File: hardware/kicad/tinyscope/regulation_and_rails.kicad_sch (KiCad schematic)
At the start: 28 parts

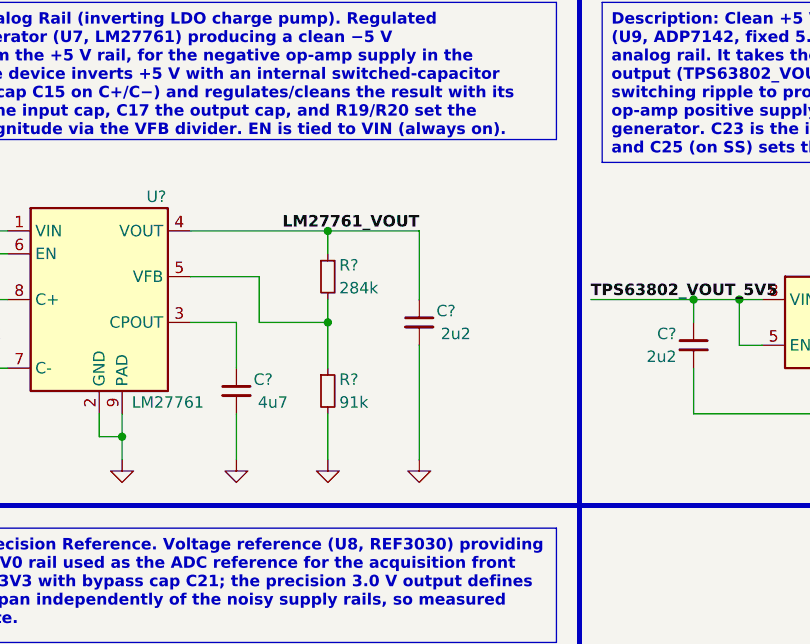
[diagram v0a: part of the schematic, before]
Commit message: feat: hardware: Adds BV199 clamps and AD8065 buffers for Front End A/B
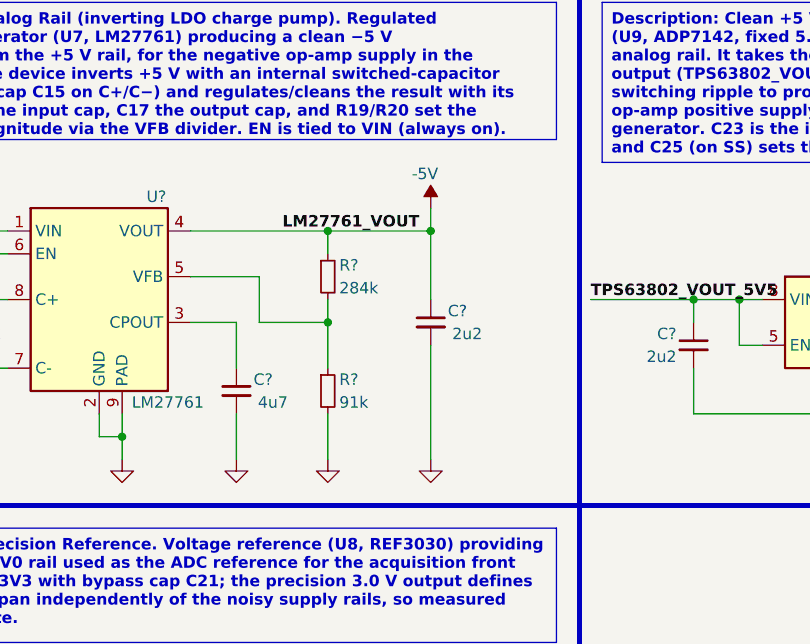
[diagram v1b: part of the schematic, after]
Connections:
- net LM27761_VOUT renamed -5V
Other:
- moved on the sheet: C?
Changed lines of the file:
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@@
   (junction (at 110.49 53.34) (diameter 0) (color 0 0 0 0)
   )
+  (junction (at 203.2 50.8) (diameter 0) (color 0 0 0 0)
+  )
   (junction (at 262.89 71.12) (diameter 0) (color 0 0 0 0)
   )
@@
     (stroke (width 0) (type default))
   )
-  (wire (pts (xy 201.93 63.5) (xy 201.93 76.2))
+  (wire (pts (xy 203.2 63.5) (xy 203.2 76.2))
     (stroke (width 0) (type default))
   )
@@
     (stroke (width 0) (type default))
   )
+  (wire (pts (xy 203.2 48.26) (xy 203.2 50.8))
+    (stroke (width 0) (type default))
+  )
   (wire (pts (xy 41.91 71.12) (xy 49.53 71.12))
     (stroke (width 0) (type default))
@@
     (stroke (width 0) (type default))
   )
-  (wire (pts (xy 191.77 50.8) (xy 201.93 50.8))
+  (wire (pts (xy 191.77 50.8) (xy 203.2 50.8))
     (stroke (width 0) (type default))
   )
@@
     (stroke (width 0) (type default))
   )
-  (wire (pts (xy 201.93 50.8) (xy 201.93 58.42))
+  (wire (pts (xy 203.2 50.8) (xy 203.2 58.42))
     (stroke (width 0) (type default))
   )
@@
     )
   )
+  (symbol (lib_id "power:-5V") (at 203.2 48.26 0) (unit 1)
+    (in_bom yes) (on_board yes) (dnp no)
+    (property "Reference" "#PWR0113" (at 203.2 45.72 0)
+      (effects (font (size 1.27 1.27)) hide)
+    )
+    (property "Value" "-5V" (at 202.565 44.45 0)
+      (effects (font (size 1.27 1.27)))
+    )
+    (property "Footprint" "" (at 203.2 48.26 0)
+      (effects (font (size 1.27 1.27)) hide)
+    )
+    (property "Datasheet" "" (at 203.2 48.26 0)
+      (effects (font (size 1.27 1.27)) hide)
+    )
+    (pin "1")
+    (instances
+      (project "tinyscope"
+        (path "/bb072e32-cc57-415a-8554-0e84d374f333/1c26ba79-0794-42b8-82e1-265696d83365"
+          (reference "#PWR0113") (unit 1)
+        )
+      )
+    )
+  )
   (symbol (lib_id "Device:C_Small") (at 110.49 58.42 0) (unit 1)
     (in_bom yes) (on_board yes) (dnp no)
@@
     )
   )
-  (symbol (lib_id "power:GND") (at 201.93 76.2 0) (unit 1)
+  (symbol (lib_id "power:GND") (at 203.2 76.2 0) (unit 1)
     (in_bom yes) (on_board yes) (dnp no) (fields_autoplaced)
-    (property "Reference" "#PWR?" (at 201.93 82.55 0)
-      (effects (font (size 1.27 1.27)) hide)
-    )
-    (property "Value" "GND" (at 201.93 81.28 0)
-      (effects (font (size 1.27 1.27)) hide)
-    )
-    (property "Footprint" "" (at 201.93 76.2 0)
-      (effects (font (size 1.27 1.27)) hide)
-    )
-    (property "Datasheet" "" (at 201.93 76.2 0)
+    (property "Reference" "#PWR?" (at 203.2 82.55 0)
+      (effects (font (size 1.27 1.27)) hide)
+    )
+    (property "Value" "GND" (at 203.2 81.28 0)
+      (effects (font (size 1.27 1.27)) hide)
+    )
+    (property "Footprint" "" (at 203.2 76.2 0)
+      (effects (font (size 1.27 1.27)) hide)
+    )
+    (property "Datasheet" "" (at 203.2 76.2 0)
       (effects (font (size 1.27 1.27)) hide)
     )
@@
     )
   )
-  (symbol (lib_id "Device:C_Small") (at 201.93 60.96 0) (unit 1)
+  (symbol (lib_id "Device:C_Small") (at 203.2 60.96 0) (unit 1)
     (in_bom yes) (on_board yes) (dnp no)
-    (property "Reference" "C?" (at 203.835 59.69 0)
+    (property "Reference" "C?" (at 205.105 59.69 0)
       (effects (font (size 1.27 1.27)) (justify left))
     )
-    (property "Value" "2u2" (at 207.645 62.23 0)
+    (property "Value" "2u2" (at 208.915 62.23 0)
       (effects (font (size 1.27 1.27)) (justify right))
     )
-    (property "Footprint" "" (at 201.93 60.96 0)
-      (effects (font (size 1.27 1.27)) hide)
-    )
-    (property "Datasheet" "~" (at 201.93 60.96 0)
-      (effects (font (size 1.27 1.27)) hide)
-    )
+    (property "Footprint" "" (at 203.2 60.96 0)
+      (effects (font (size 1.27 1.27)) hide)
+    )
+    (property "Datasheet" "~" (at 203.2 60.96 0)
+      (effects (font (size 1.27 1.27)) hide)
+    )

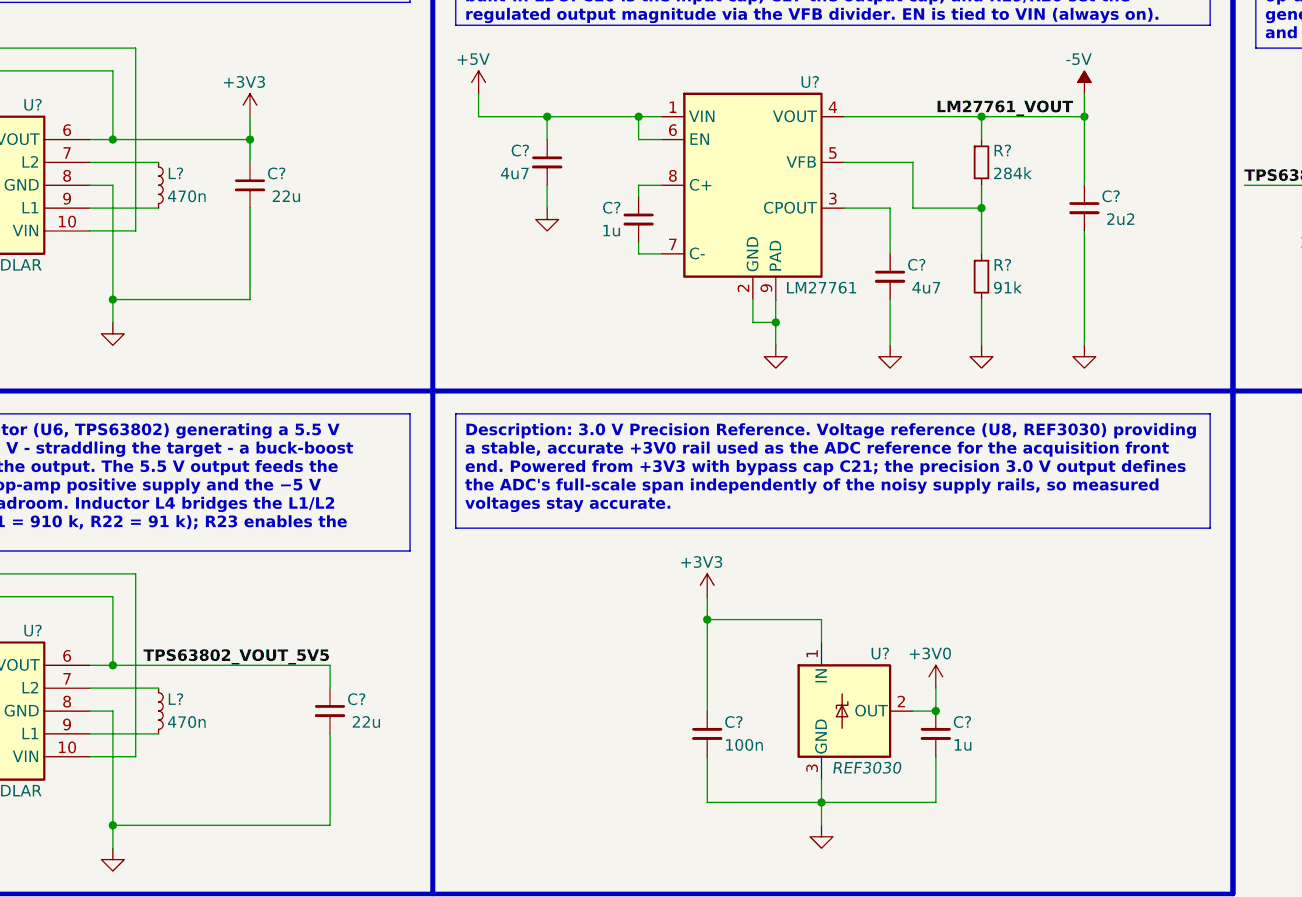
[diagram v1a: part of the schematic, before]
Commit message: feat: hardware: Adds Waveshare 16498 display 02x17 connector. Cleans up all schematics
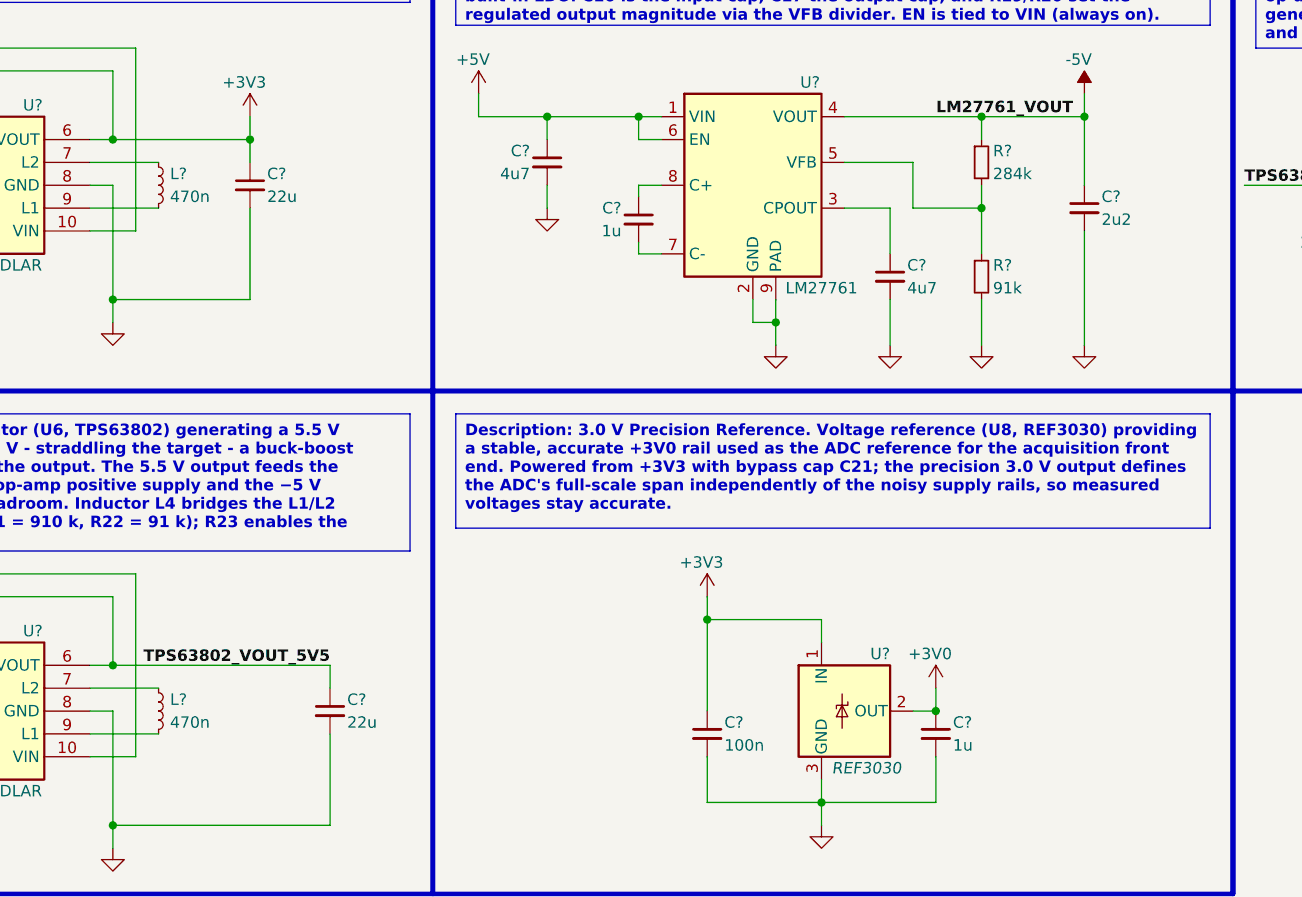
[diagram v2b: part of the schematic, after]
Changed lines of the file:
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@@
       (effects (font (size 1.27 1.27)) (justify left))
     )
-    (property "Value" "22u" (at 116.205 59.69 0)
-      (effects (font (size 1.27 1.27)) (justify right))
+    (property "Value" "22u" (at 112.395 59.69 0)
+      (effects (font (size 1.27 1.27)) (justify left))
     )
     (property "Footprint" "" (at 110.49 58.42 0)
@@
   (symbol (lib_id "Device:L_Small") (at 100.33 116.84 0) (unit 1)
     (in_bom yes) (on_board yes) (dnp no)
-    (property "Reference" "L?" (at 102.235 115.57 0)
-      (effects (font (size 1.27 1.27)))
-    )
-    (property "Value" "470n" (at 103.505 118.11 0)
-      (effects (font (size 1.27 1.27)))
+    (property "Reference" "L?" (at 101.6 115.57 0)
+      (effects (font (size 1.27 1.27)) (justify left))
+    )
+    (property "Value" "470n" (at 101.6 118.11 0)
+      (effects (font (size 1.27 1.27)) (justify left))
     )
     (property "Footprint" "" (at 100.33 116.84 0)
@@
       (effects (font (size 1.27 1.27)) (justify left))
     )
-    (property "Value" "2u2" (at 208.915 62.23 0)
-      (effects (font (size 1.27 1.27)) (justify right))
+    (property "Value" "2u2" (at 205.105 62.23 0)
+      (effects (font (size 1.27 1.27)) (justify left))
     )
     (property "Footprint" "" (at 203.2 60.96 0)
@@
   (symbol (lib_id "Device:L_Small") (at 100.33 58.42 0) (unit 1)
     (in_bom yes) (on_board yes) (dnp no)
-    (property "Reference" "L?" (at 102.235 57.15 0)
-      (effects (font (size 1.27 1.27)))
-    )
-    (property "Value" "470n" (at 103.505 59.69 0)
-      (effects (font (size 1.27 1.27)))
+    (property "Reference" "L?" (at 101.6 57.15 0)
+      (effects (font (size 1.27 1.27)) (justify left))
+    )
+    (property "Value" "470n" (at 101.6 59.69 0)
+      (effects (font (size 1.27 1.27)) (justify left))
     )
     (property "Footprint" "" (at 100.33 58.42 0)
@@
       (effects (font (size 1.27 1.27)) (justify left))
     )
-    (property "Value" "22u" (at 125.095 118.11 0)
-      (effects (font (size 1.27 1.27)) (justify right))
+    (property "Value" "22u" (at 121.285 118.11 0)
+      (effects (font (size 1.27 1.27)) (justify left))
     )
     (property "Footprint" "" (at 119.38 116.84 0)
@@
       (effects (font (size 1.27 1.27)) (justify left))
     )
-    (property "Value" "4u7" (at 187.325 69.85 0)
-      (effects (font (size 1.27 1.27)) (justify right))
+    (property "Value" "4u7" (at 183.515 69.85 0)
+      (effects (font (size 1.27 1.27)) (justify left))
     )
     (property "Footprint" "" (at 181.61 68.58 0)

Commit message: feat: hardware: Add global labels on power and charging, and regulation and rails subschematics
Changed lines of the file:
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@@
   (junction (at 153.67 50.8) (diameter 0) (color 0 0 0 0)
   )
-  (junction (at 41.91 43.18) (diameter 0) (color 0 0 0 0)
-  )
   (junction (at 49.53 71.12) (diameter 0) (color 0 0 0 0)
   )
@@
   (junction (at 262.89 58.42) (diameter 0) (color 0 0 0 0)
   )
-  (junction (at 41.91 101.6) (diameter 0) (color 0 0 0 0)
-  )
   (junction (at 95.25 129.54) (diameter 0) (color 0 0 0 0)
   )
@@
     (stroke (width 0) (type default))
   )
-  (wire (pts (xy 26.67 43.18) (xy 41.91 43.18))
-    (stroke (width 0) (type default))
-  )
   (wire (pts (xy 59.69 63.5) (xy 64.77 63.5))
     (stroke (width 0) (type default))
@@
   )
   (wire (pts (xy 92.71 58.42) (xy 95.25 58.42))
-    (stroke (width 0) (type default))
-  )
-  (wire (pts (xy 26.67 101.6) (xy 41.91 101.6))
     (stroke (width 0) (type default))
   )
@@
     (effects (font (size 4 4) (thickness 0.254) bold (color 0 0 0 1)) (justify left bottom))
   )
-  (label "BQ24075_OUT" (at 26.67 101.6 0) (fields_autoplaced)
-    (effects (font (size 1.27 1.27) bold) (justify left bottom))
-  )
   (label "TPS63802_VOUT_5V5" (at 220.98 58.42 0) (fields_autoplaced)
     (effects (font (size 1.27 1.27) bold) (justify left bottom))
@@
     (effects (font (size 1.27 1.27) bold) (justify right bottom))
   )
-  (label "BQ24075_OUT" (at 26.67 43.18 0) (fields_autoplaced)
-    (effects (font (size 1.27 1.27) bold) (justify left bottom))
-  )
   (label "TPS63802_VOUT_5V5" (at 119.38 111.76 180) (fields_autoplaced)
     (effects (font (size 1.27 1.27) bold) (justify right bottom))
   )
+  (global_label "BQ24075_OUT" (shape bidirectional) (at 41.91 101.6 180) (fields_autoplaced)
+    (effects (font (size 1.27 1.27)) (justify right))
+    (property "Intersheetrefs" "${INTERSHEET_REFS}" (at 24.6487 101.6 0)
+      (effects (font (size 1.27 1.27)) (justify right) hide)
+    )
+  )
+  (global_label "BQ24075_OUT" (shape bidirectional) (at 41.91 43.18 180) (fields_autoplaced)
+    (effects (font (size 1.27 1.27)) (justify right))
+    (property "Intersheetrefs" "${INTERSHEET_REFS}" (at 24.6487 43.18 0)
+      (effects (font (size 1.27 1.27)) (justify right) hide)
+    )
+  )
   (symbol (lib_id "Device:C_Small") (at 153.67 62.23 0) (unit 1)

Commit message: fix: hardware: Solves electrical rules warnings and errors #7
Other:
- moved on the sheet: C?, U?

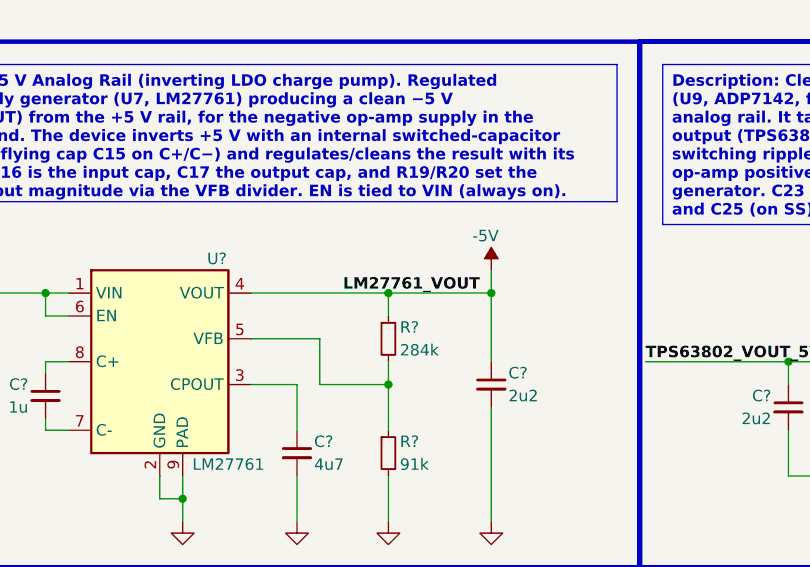
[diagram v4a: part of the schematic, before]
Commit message: fix: hardware: Solves electrical rules warnings and errors #9
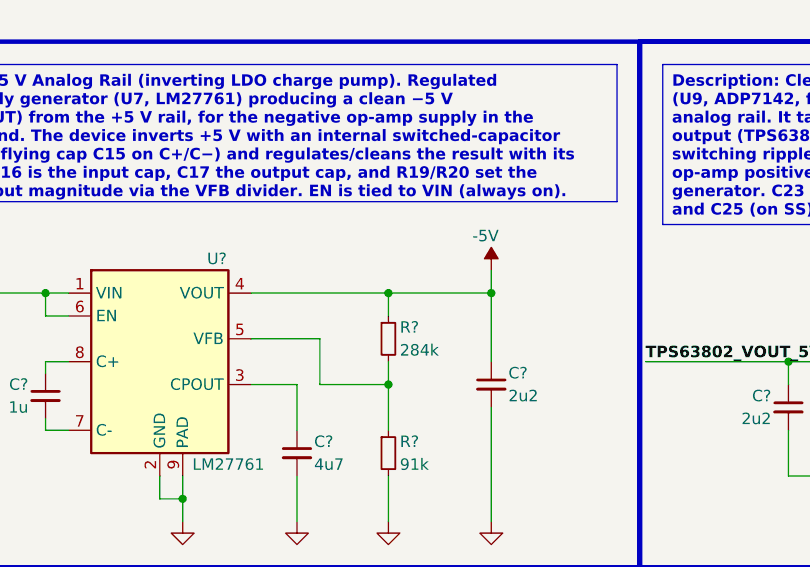
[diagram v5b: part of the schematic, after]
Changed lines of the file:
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@@
     (effects (font (size 1.27 1.27) bold) (justify left bottom))
-  )
-  (label "LM27761_VOUT" (at 201.93 50.8 180) (fields_autoplaced)
-    (effects (font (size 1.27 1.27) bold) (justify right bottom))
   )
   (label "TPS63802_VOUT_5V5" (at 119.38 111.76 180) (fields_autoplaced)

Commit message: feat: hardware: Assigns footprints for resistors
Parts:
- R? (x8): footprint (none) -> Resistor_SMD:R_0402_1005Metric
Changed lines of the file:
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@@
       (effects (font (size 1.27 1.27)) (justify left))
     )
-    (property "Footprint" "" (at 191.77 55.88 0)
+    (property "Footprint" "Resistor_SMD:R_0402_1005Metric" (at 191.77 55.88 0)
       (effects (font (size 1.27 1.27)) hide)
     )
@@
       (effects (font (size 1.27 1.27)) (justify right))
     )
-    (property "Footprint" "" (at 49.53 124.46 0)
+    (property "Footprint" "Resistor_SMD:R_0402_1005Metric" (at 49.53 124.46 0)
       (effects (font (size 1.27 1.27)) hide)
     )
@@
       (effects (font (size 1.27 1.27)) (justify right))
     )
-    (property "Footprint" "" (at 59.69 109.22 0)
+    (property "Footprint" "Resistor_SMD:R_0402_1005Metric" (at 59.69 109.22 0)
       (effects (font (size 1.27 1.27)) hide)
     )
@@
       (effects (font (size 1.27 1.27)) (justify right))
     )
-    (property "Footprint" "" (at 49.53 114.3 0)
+    (property "Footprint" "Resistor_SMD:R_0402_1005Metric" (at 49.53 114.3 0)
       (effects (font (size 1.27 1.27)) hide)
     )
@@
       (effects (font (size 1.27 1.27)) (justify right))
     )
-    (property "Footprint" "" (at 49.53 55.88 0)
+    (property "Footprint" "Resistor_SMD:R_0402_1005Metric" (at 49.53 55.88 0)
       (effects (font (size 1.27 1.27)) hide)
     )
@@
       (effects (font (size 1.27 1.27)) (justify left))
     )
-    (property "Footprint" "" (at 191.77 68.58 0)
+    (property "Footprint" "Resistor_SMD:R_0402_1005Metric" (at 191.77 68.58 0)
       (effects (font (size 1.27 1.27)) hide)
     )
@@
       (effects (font (size 1.27 1.27)) (justify right))
     )
-    (property "Footprint" "" (at 59.69 50.8 0)
+    (property "Footprint" "Resistor_SMD:R_0402_1005Metric" (at 59.69 50.8 0)
       (effects (font (size 1.27 1.27)) hide)
     )
@@
       (effects (font (size 1.27 1.27)) (justify right))
     )
-    (property "Footprint" "" (at 49.53 66.04 0)
-      (effects (font (size 1.27 1.27)) hide)
-    )
+    (property "Footprint" "Resistor_SMD:R_0402_1005Metric" (at 49.53 66.04 0)
+      (effects (font (size 1.27 1.27)) hide)
+    )
